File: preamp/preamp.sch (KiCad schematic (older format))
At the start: 38 parts, among them P1 Plug salida, U1 N35532, U2 N35532

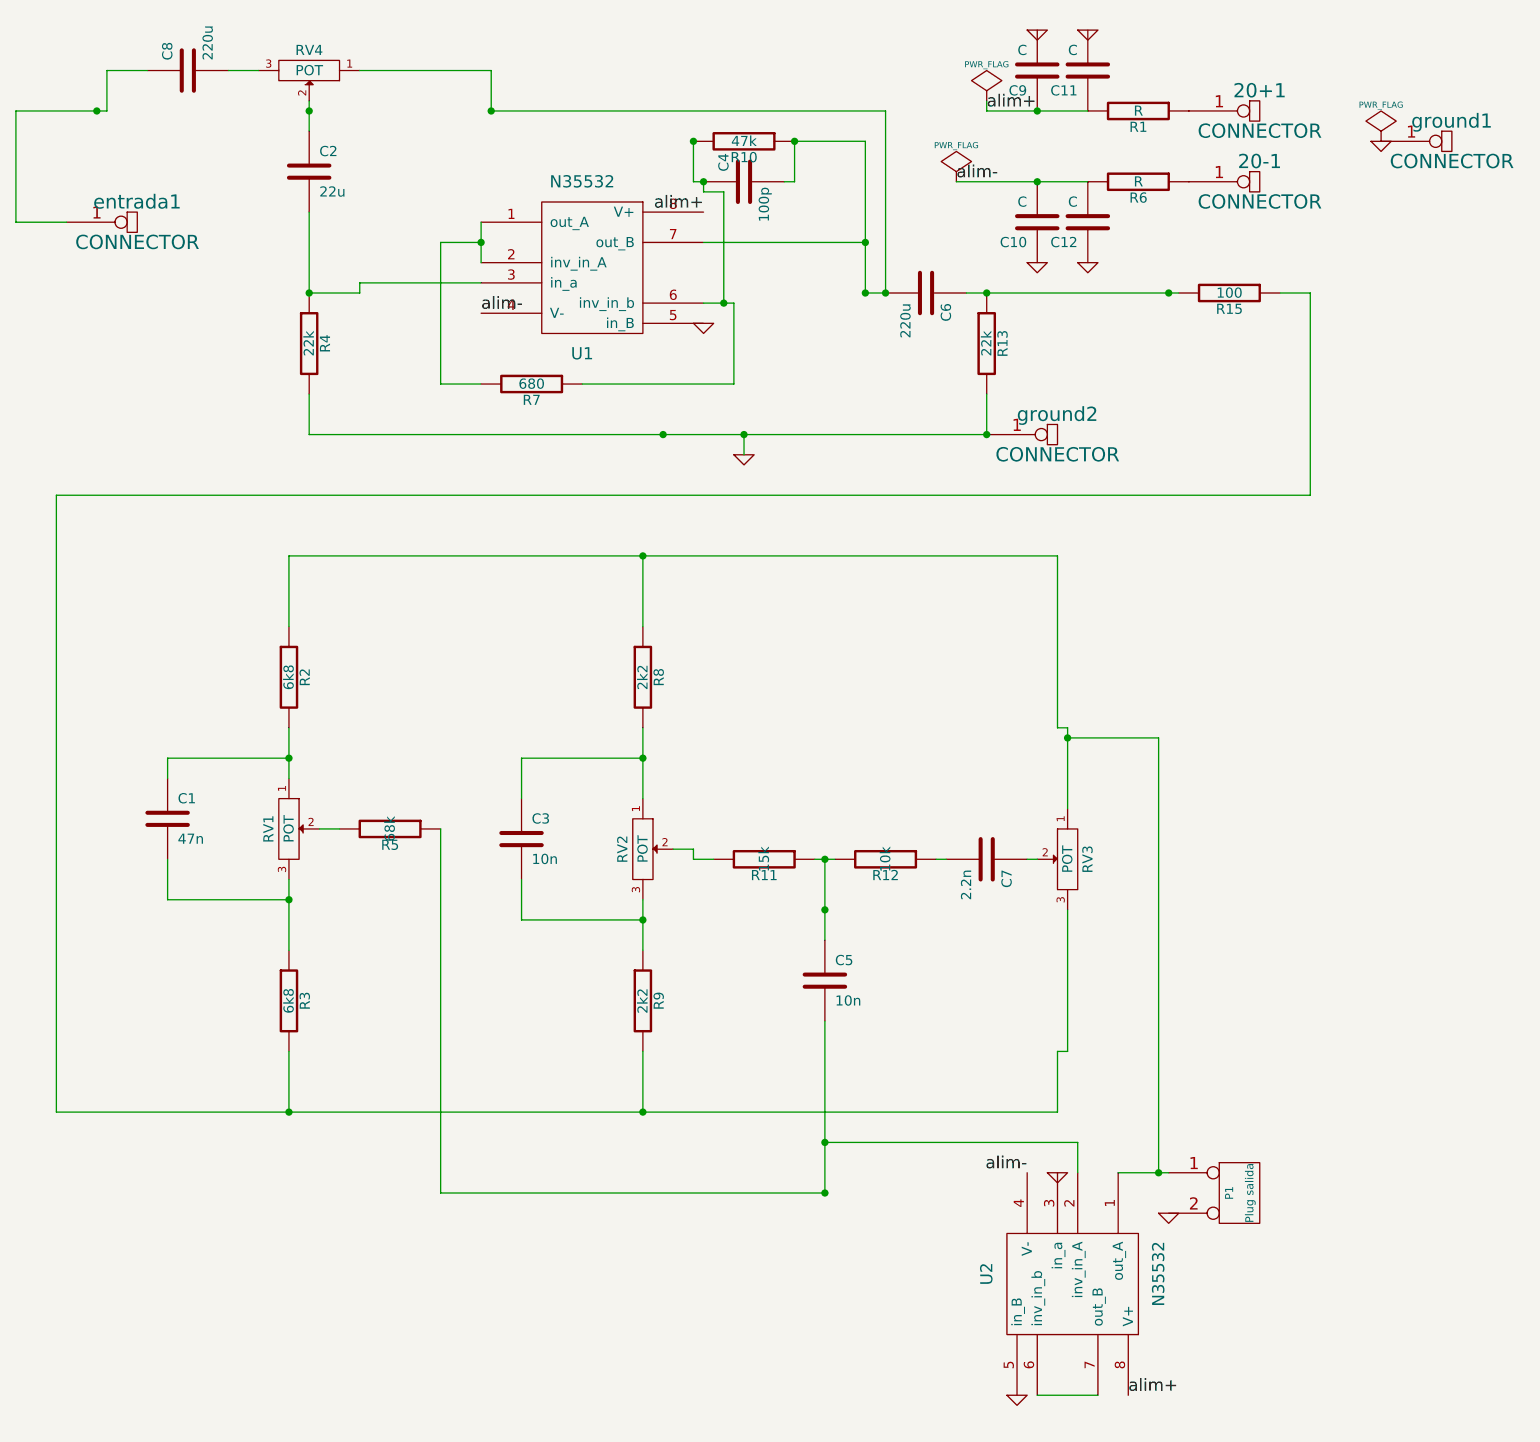
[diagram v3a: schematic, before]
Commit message: 
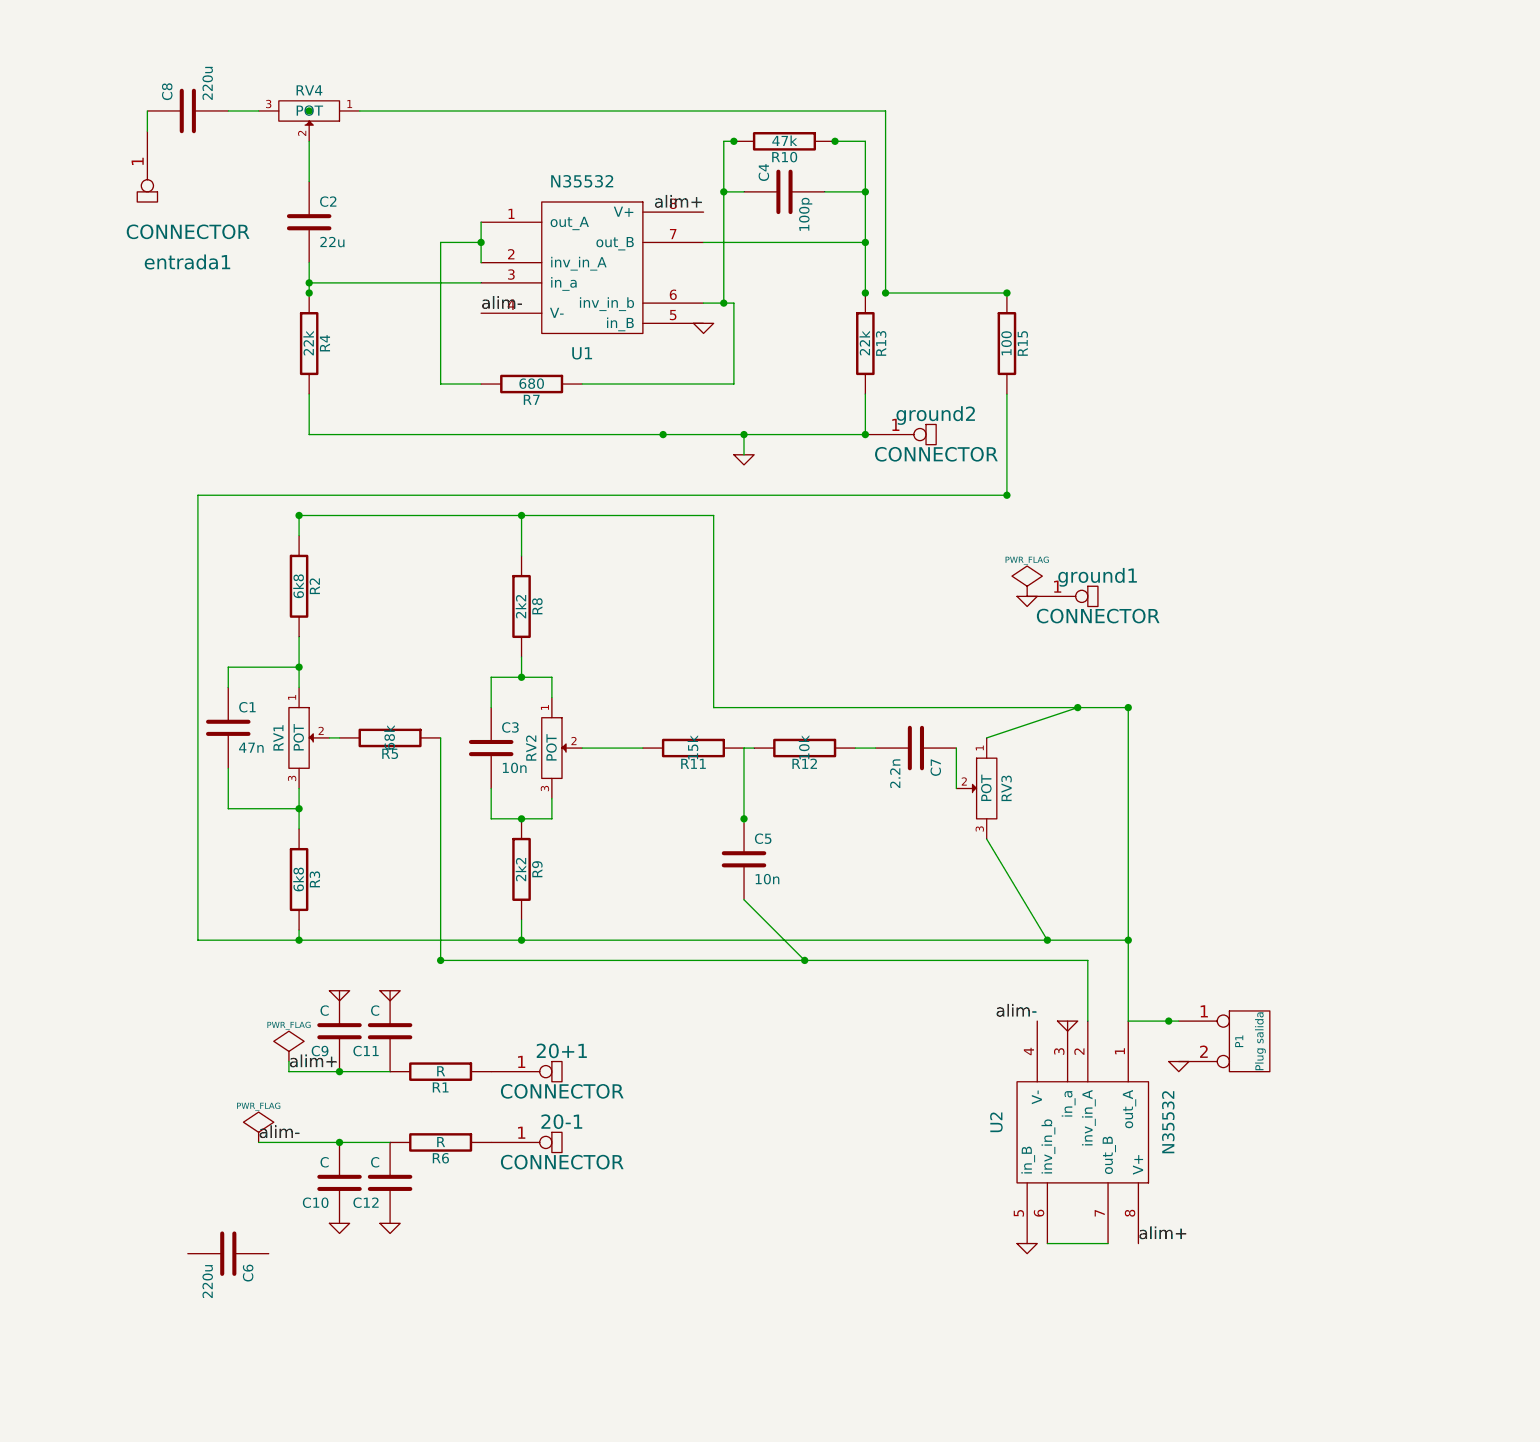
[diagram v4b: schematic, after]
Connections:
- net at P1.1 (P1), R2.1, R8.1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: now also R15.2, R3.2, R9.2, RV3.3
- net at C4.2, R10.1, U1.7 (out_B): now also R13.1; no longer C6.2, RV4.1
- new net: R15.1, RV4.1
- now unconnected: C6.1
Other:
- moved on the sheet: 20+1, 20-1, C1, C10, C11, C12, C2, C3, C4, C5, C6, C7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
